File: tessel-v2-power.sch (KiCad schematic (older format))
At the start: 56 parts, among them J301 CONN_01X02, Q301 MMSS8550, U301 AAT4610, U302 AAT4610, U303 AP3417C, U304 AP3417C, U305 AP3418

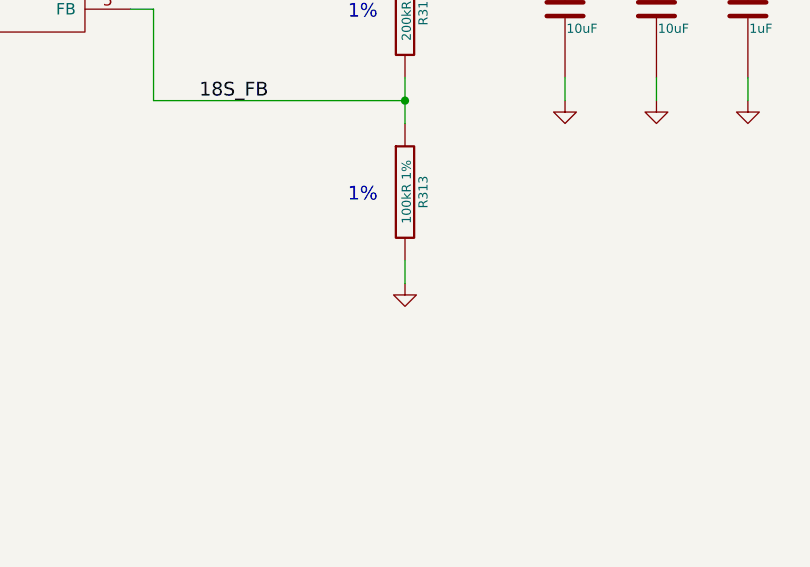
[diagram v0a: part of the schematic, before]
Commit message: swapped led resistor values, package for some dnps, exported to cmp and net
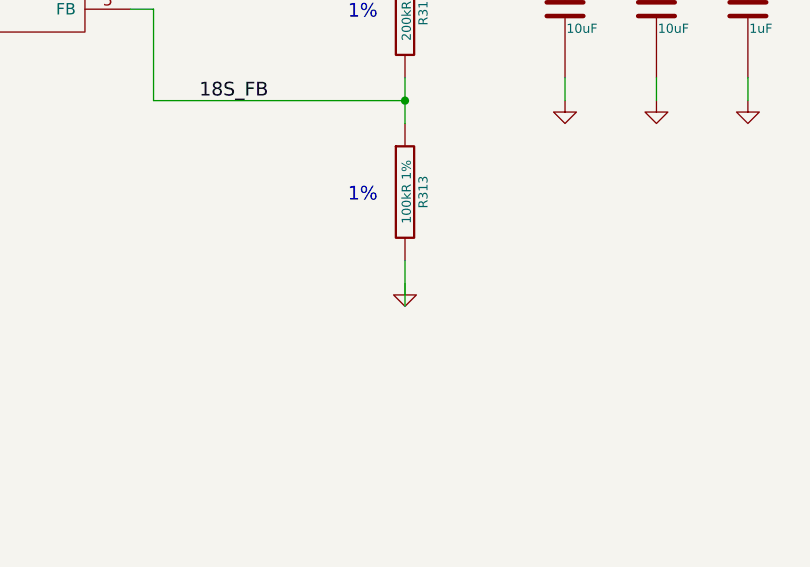
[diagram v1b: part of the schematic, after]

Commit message: led and related resistor changeover
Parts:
- R305, R306: value 1kR -> 120R
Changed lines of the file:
@@
 P 5000 6500
 F 0 "R305" V 5080 6500 40  0000 C CNN
-F 1 "1kR" V 5007 6501 40  0000 C CNN
+F 1 "120R" V 5007 6501 40  0000 C CNN
 F 2 "tm-kicad-lib:SMD-0402-R" V 4930 6500 30  0001 C CNN
 F 3 "" H 5000 6500 30  0000 C CNN
@@
 P 5000 9100
 F 0 "R306" V 5080 9100 40  0000 C CNN
-F 1 "1kR" V 5007 9101 40  0000 C CNN
+F 1 "120R" V 5007 9101 40  0000 C CNN
 F 2 "tm-kicad-lib:SMD-0402-R" V 4930 9100 30  0001 C CNN
 F 3 "" H 5000 9100 30  0000 C CNN

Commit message: swapped load switches
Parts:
- removed U301, U302: AAT4610, Housings_SOT-23_SOT-143_TSOT-6:SOT-23-5, symbol AAT4610
- added U301, U302: MT9700, symbol MT9700
- R303, R304: value 33kR -> 27kR
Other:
- note added: "I_SET = 6.8kV/R_SET\n6.8kV/27kR = 252mA"
- note removed: "R_SET I_LIM\n---------\n56kR : 150mA\n33kR : 250mA\n10kR : 750mA"
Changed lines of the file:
@@
-$EndComp
-$Comp
-L AAT4610 U301
-U 1 1 548FCFA8
-P 3400 5700
-F 0 "U301" H 3050 5950 60  0000 C CNN
-F 1 "AAT4610" H 3400 5700 60  0000 C CNN
-F 2 "Housings_SOT-23_SOT-143_TSOT-6:SOT-23-5" H 3400 5700 60  0001 C CNN
-F 3 "" H 3400 5700 60  0000 C CNN
-	1    3400 5700
-	1    0    0    -1
 $EndComp
 $Comp
@@
 P 2700 6200
 F 0 "R303" V 2780 6200 40  0000 C CNN
-F 1 "33kR" V 2707 6201 40  0000 C CNN
+F 1 "27kR" V 2707 6201 40  0000 C CNN
 F 2 "tm-kicad-lib:SMD-0402-R" V 2630 6200 30  0001 C CNN
 F 3 "" H 2700 6200 30  0000 C CNN
@@
 	1    0    0    -1
 $EndComp
-Text Notes 3050 6400 0    60   ~ 0
-R_SET  I_LIM\n---------\n56kR : 150mA\n33kR : 250mA\n10kR : 750mA
+Text Notes 2900 6300 0    60   ~ 0
+I_SET = 6.8kV/R_SET\n6.8kV/27kR = 252mA
 $Comp
 L TM_C C315
@@
 3.3V_PORT_B
 $Comp
-L AAT4610 U302
-U 1 1 54BD9A8A
-P 3400 8300
-F 0 "U302" H 3050 8550 60  0000 C CNN
-F 1 "AAT4610" H 3400 8300 60  0000 C CNN
-F 2 "Housings_SOT-23_SOT-143_TSOT-6:SOT-23-5" H 3400 8300 60  0001 C CNN
-F 3 "" H 3400 8300 60  0000 C CNN
-	1    3400 8300
-	1    0    0    -1
-$EndComp
-$Comp
 L GND #PWR080
 U 1 1 54BD9A90
@@
 P 2700 8800
 F 0 "R304" V 2780 8800 40  0000 C CNN
-F 1 "33kR" V 2707 8801 40  0000 C CNN
+F 1 "27kR" V 2707 8801 40  0000 C CNN
 F 2 "tm-kicad-lib:SMD-0402-R" V 2630 8800 30  0001 C CNN
 F 3 "" H 2700 8800 30  0000 C CNN
@@
 	1    0    0    -1
 $EndComp
-Text Notes 3050 9000 0    60   ~ 0
-R_SET  I_LIM\n---------\n56kR : 150mA\n33kR : 250mA\n10kR : 750mA
 Text GLabel 2600 8200 0    60   Input ~ 0
 3.3V_CP
@@
 Connection ~ 15300 5700
 Connection ~ 11500 9400
+$Comp
+L MT9700 U301
+U 1 1 5514ACA5
+P 3400 5700
+F 0 "U301" H 3100 5950 60  0000 C CNN
+F 1 "MT9700" H 3400 5700 60  0000 C CNN
+F 2 "" H 3400 5700 60  0000 C CNN
+F 3 "" H 3400 5700 60  0000 C CNN
+	1    3400 5700
+	1    0    0    -1
+$EndComp
+$Comp
+L MT9700 U302
+U 1 1 5514AD5E
+P 3400 8300
+F 0 "U302" H 3100 8550 60  0000 C CNN
+F 1 "MT9700" H 3400 8300 60  0000 C CNN
+F 2 "" H 3400 8300 60  0000 C CNN
+F 3 "" H 3400 8300 60  0000 C CNN
+	1    3400 8300
+	1    0    0    -1
+$EndComp
+Text Notes 2900 8900 0    60   ~ 0
+I_SET = 6.8kV/R_SET\n6.8kV/27kR = 252mA
 $EndSCHEMATC

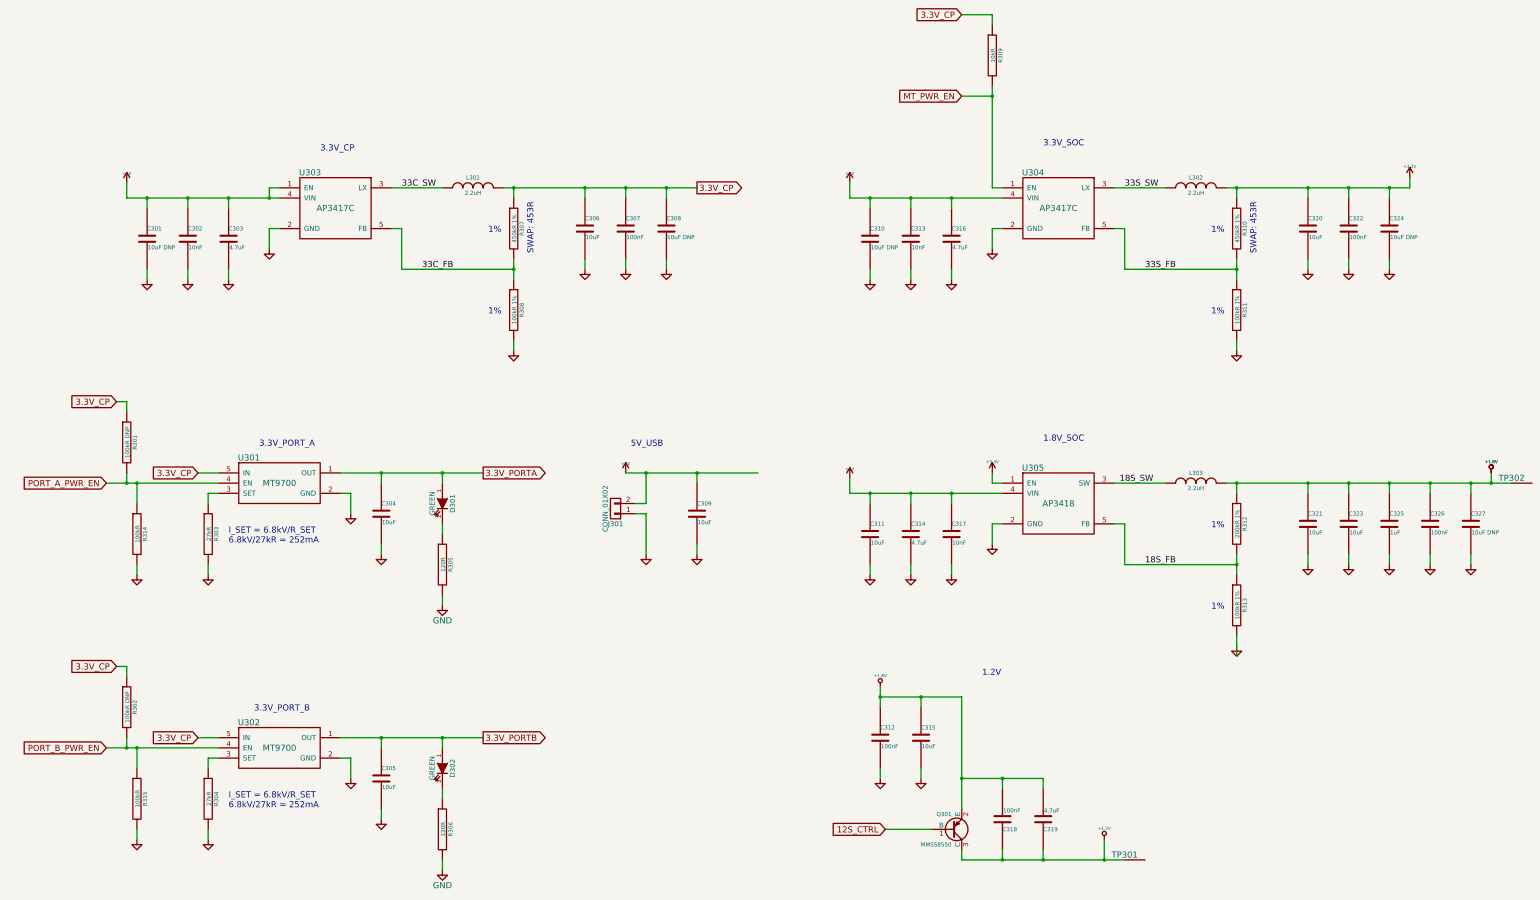
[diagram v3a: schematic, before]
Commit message: swapped to a single 33 regulator...
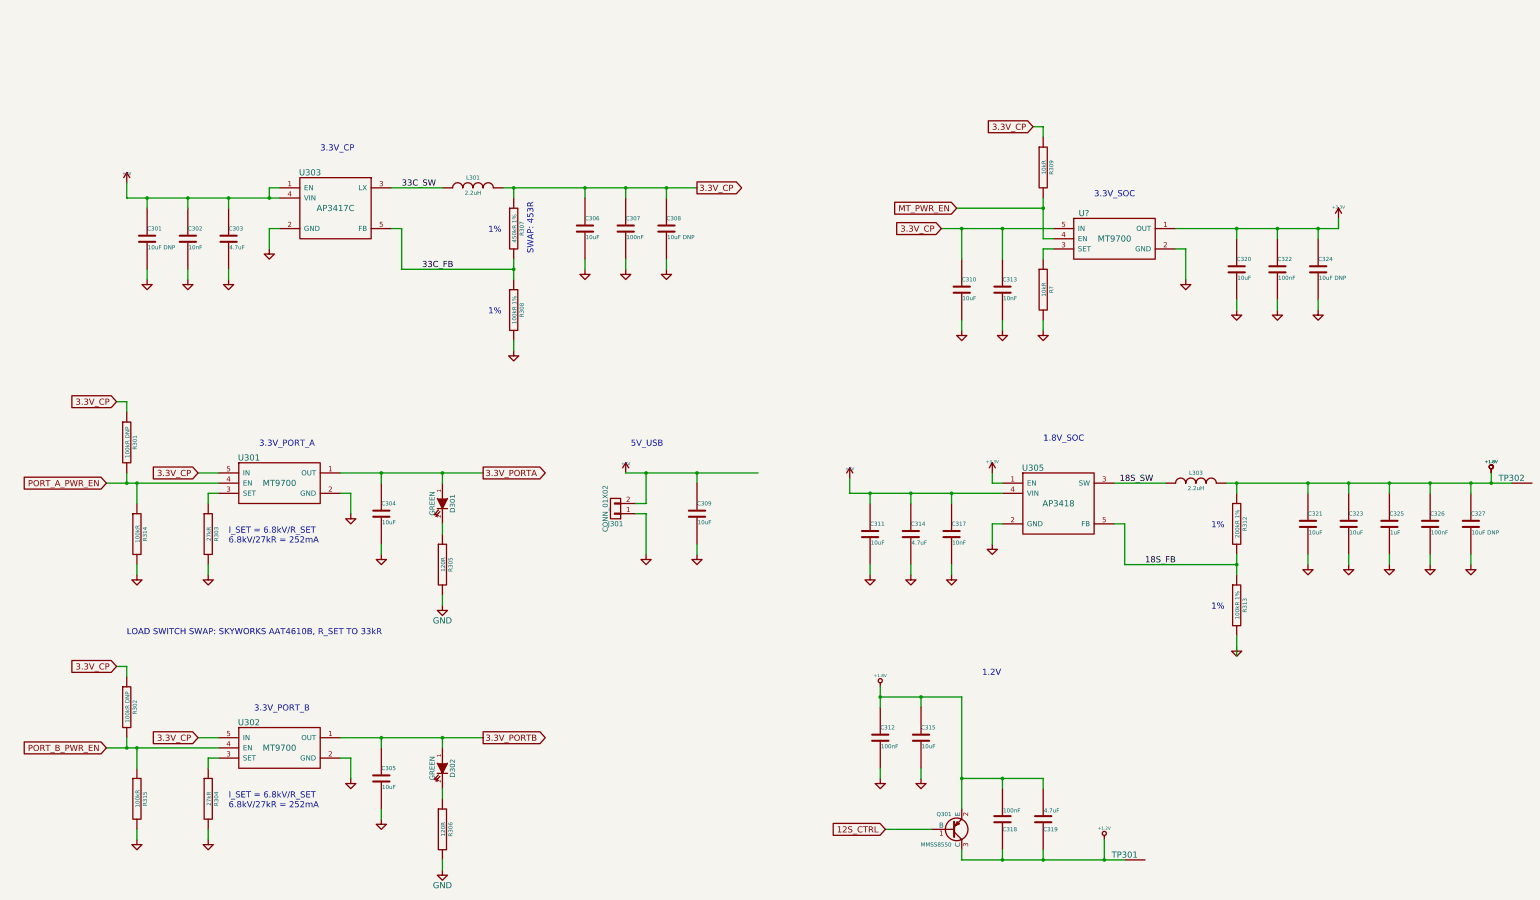
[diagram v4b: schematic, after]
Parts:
- removed C316: 4.7uF, tm-kicad-lib:SMD-0603-C, symbol TM_C
- removed L302: 2.2uH, tm-kicad-lib:SWPA5020S, symbol TM_L
- removed R310: 450kR 1%, tm-kicad-lib:SMD-0402-R, symbol TM_R
- removed R311: 100kR 1%, tm-kicad-lib:SMD-0402-R, symbol TM_R
- removed U304: AP3417C, Housings_SOT-23_SOT-143_TSOT-6:SOT-23-5, symbol AP3417C
- added R?: 10kR, tm-kicad-lib:SMD-0402-R, symbol TM_R
- added U?: MT9700, symbol MT9700
- C310: value 10uF DNP -> 10uF
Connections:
- net +3V3: now also U?.1 (OUT)
- net +5V: no longer C310.1, C313.1
- net 3.3V_CP: now also C310.1, C313.1, U?.5 (IN)
- net GND: now also R?.2, U?.2 (GND)
- net MT_PWR_EN: now also U?.4 (EN)
- new net: R?.1, U?.3 (SET)
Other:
- note added: "LOAD SWITCH SWAP: SKYWORKS AAT4610B, R_SET TO 33kR"
- moved on the sheet: C310, C313, C320, C322, C324, R309

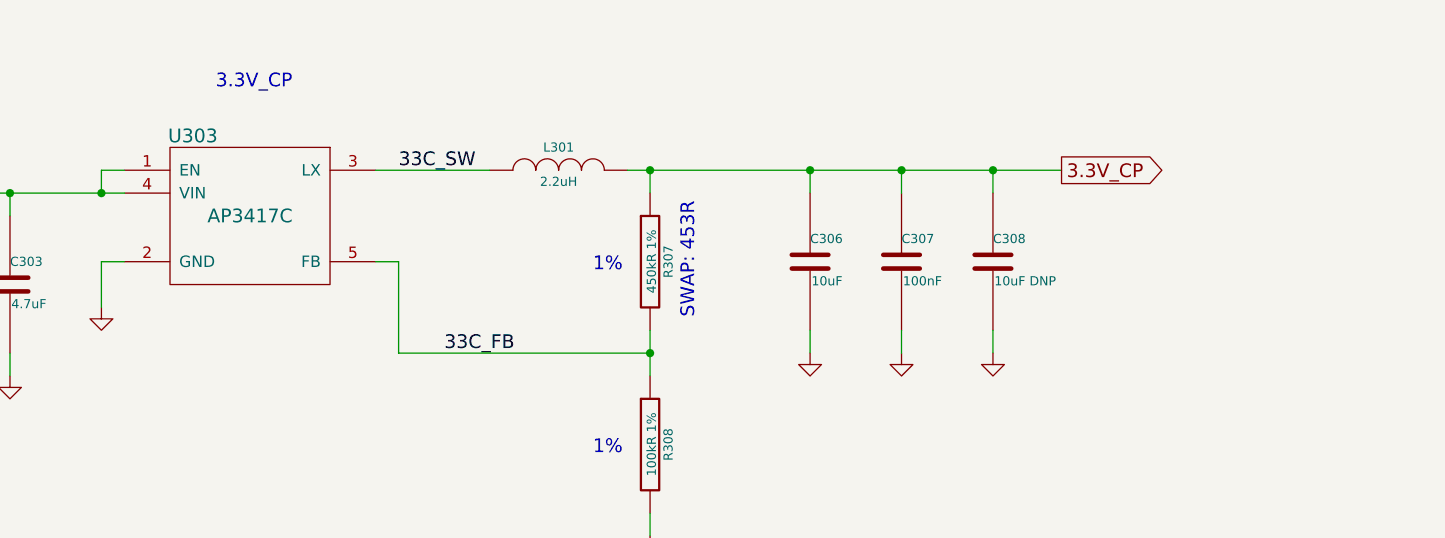
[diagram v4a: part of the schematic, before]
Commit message: more caps
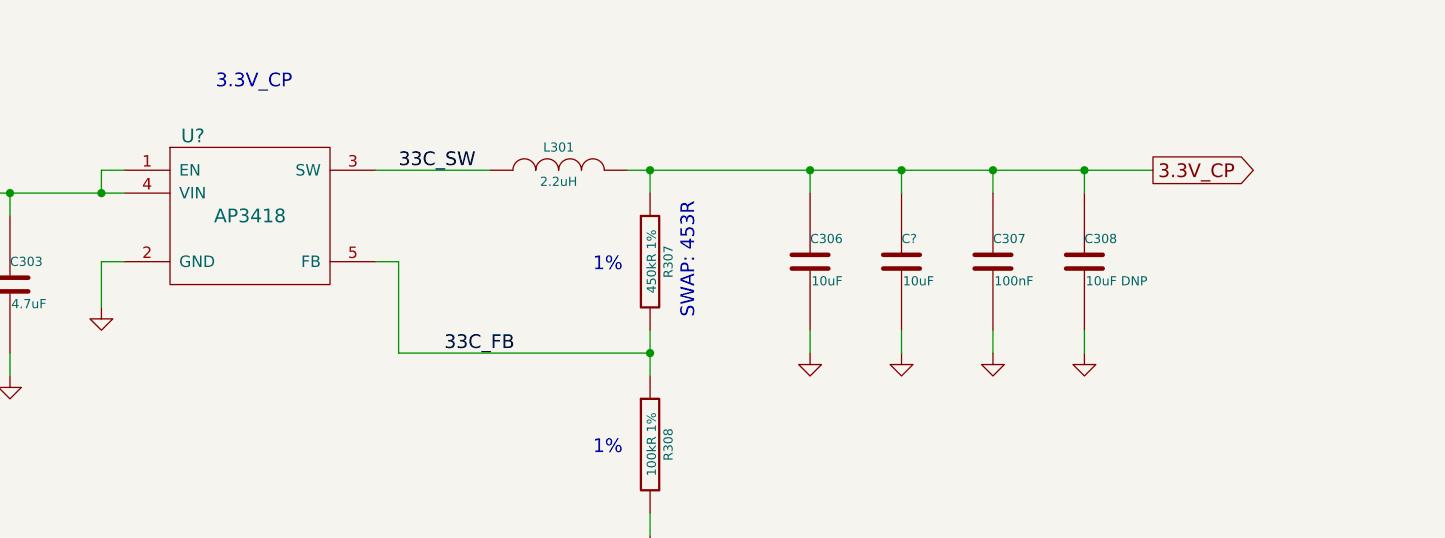
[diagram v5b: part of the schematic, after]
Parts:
- removed U303: AP3417C, Housings_SOT-23_SOT-143_TSOT-6:SOT-23-5, symbol AP3417C
- added C?: 10uF, tm-kicad-lib:SMD-0805-C, symbol TM_C
- added U?: AP3418, Housings_SOT-23_SOT-143_TSOT-6:SOT-23-5, symbol AP3418
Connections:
- net +5V: now also U?.1 (EN), U?.4 (VIN)
- net 3.3V_CP: now also C?.1
- net 33C_FB: now also U?.5 (FB)
- net 33C_SW: now also U?.3 (SW)
- net GND: now also C?.2, U?.2 (GND)
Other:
- moved on the sheet: C307, C308
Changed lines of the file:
@@
 L TM_C C308
 U 1 1 549071E4
-P 7200 3200
-F 0 "C308" H 7200 3300 40  0000 L CNN
-F 1 "10uF DNP" H 7206 3115 40  0000 L CNN
-F 2 "tm-kicad-lib:SMD-0805-C" H 7238 3050 30  0001 C CNN
-F 3 "" H 7200 3200 60  0000 C CNN
-	1    7200 3200
+P 7600 3200
+F 0 "C308" H 7600 3300 40  0000 L CNN
+F 1 "10uF DNP" H 7606 3115 40  0000 L CNN
+F 2 "tm-kicad-lib:SMD-0805-C" H 7638 3050 30  0001 C CNN
+F 3 "" H 7600 3200 60  0000 C CNN
+	1    7600 3200
 	1    0    0    -1
 $EndComp
@@
 L TM_C C307
 U 1 1 549071F0
-P 6800 3200
-F 0 "C307" H 6800 3300 40  0000 L CNN
-F 1 "100nF" H 6806 3115 40  0000 L CNN
-F 2 "tm-kicad-lib:SMD-0402-C" H 6838 3050 30  0001 C CNN
-F 3 "" H 6800 3200 60  0000 C CNN
-	1    6800 3200
+P 7200 3200
+F 0 "C307" H 7200 3300 40  0000 L CNN
+F 1 "100nF" H 7206 3115 40  0000 L CNN
+F 2 "tm-kicad-lib:SMD-0402-C" H 7238 3050 30  0001 C CNN
+F 3 "" H 7200 3200 60  0000 C CNN
+	1    7200 3200
 	1    0    0    -1
 $EndComp
@@
 L GND #PWR065
 U 1 1 54907210
-P 6800 3600
-F 0 "#PWR065" H 6800 3600 30  0001 C CNN
-F 1 "GND" H 6800 3530 30  0001 C CNN
-F 2 "" H 6800 3600 60  0000 C CNN
-F 3 "" H 6800 3600 60  0000 C CNN
-	1    6800 3600
-	1    0    0    -1
-$EndComp
-$Comp
-L GND #PWR066
-U 1 1 54907216
 P 7200 3600
-F 0 "#PWR066" H 7200 3600 30  0001 C CNN
+F 0 "#PWR065" H 7200 3600 30  0001 C CNN
 F 1 "GND" H 7200 3530 30  0001 C CNN
 F 2 "" H 7200 3600 60  0000 C CNN
 F 3 "" H 7200 3600 60  0000 C CNN
 	1    7200 3600
+	1    0    0    -1
+$EndComp
+$Comp
+L GND #PWR066
+U 1 1 54907216
+P 7600 3600
+F 0 "#PWR066" H 7600 3600 30  0001 C CNN
+F 1 "GND" H 7600 3530 30  0001 C CNN
+F 2 "" H 7600 3600 60  0000 C CNN
+F 3 "" H 7600 3600 60  0000 C CNN
+	1    7600 3600
 	1    0    0    -1
 $EndComp
@@
 $EndComp
 $Comp
-L AP3417C U303
-U 1 1 54BDB3A5
-P 3950 3000
-F 0 "U303" H 3700 3350 60  0000 C CNN
-F 1 "AP3417C" H 3950 3000 60  0000 C CNN
-F 2 "Housings_SOT-23_SOT-143_TSOT-6:SOT-23-5" H 3950 3000 60  0001 C CNN
-F 3 "http://diodes.com/datasheets/AP3417C.pdf" H 3950 3000 60  0001 C CNN
-	1    3950 3000
-	1    0    0    -1
-$EndComp
-$Comp
 L GND #PWR083
 U 1 1 54927708
@@
 	1    0    0    -1
 $EndComp
-Text GLabel 7500 2800 2    60   Output ~ 0
+Text GLabel 7900 2800 2    60   Output ~ 0
 3.3V_CP
 $Comp
@@
 Wire Wire Line
 	2100 3000 2100 2900
+Connection ~ 7600 2800
+Wire Wire Line
+	5700 4300 5700 4400
+Wire Wire Line
+	7600 3500 7600 3600
+Wire Wire Line
+	7200 3500 7200 3600
+Wire Wire Line
+	6400 3500 6400 3600
 Connection ~ 7200 2800
 Wire Wire Line
-	5700 4300 5700 4400
-Wire Wire Line
-	7200 3500 7200 3600
-Wire Wire Line
-	6800 3500 6800 3600
-Wire Wire Line
-	6400 3500 6400 3600
-Connection ~ 6800 2800
+	7600 2800 7600 2900
+Connection ~ 6400 2800
 Wire Wire Line
 	7200 2800 7200 2900
-Connection ~ 6400 2800
-Wire Wire Line
-	6800 2800 6800 2900
 Connection ~ 5700 2800
 Wire Wire Line
@@
 	5700 2800 6400 2800
 Wire Wire Line
-	6400 2800 6800 2800
-Wire Wire Line
-	6800 2800 7200 2800
-Wire Wire Line
-	7200 2800 7500 2800
+	6400 2800 7200 2800
+Wire Wire Line
+	7200 2800 7600 2800
+Wire Wire Line
+	7600 2800 7900 2800
 Connection ~ 5700 3600
 Wire Wire Line
@@
 Wire Wire Line
 	12800 3900 12800 4000
+$Comp
+L AP3418 U?
+U 1 1 5514F328
+P 3950 3000
+F 0 "U?" H 3700 3350 60  0000 C CNN
+F 1 "AP3418" H 3950 3000 60  0000 C CNN
+F 2 "Housings_SOT-23_SOT-143_TSOT-6:SOT-23-5" H 3950 3000 60  0001 C CNN
+F 3 "http://diodes.com/datasheets/AP3418.pdf" H 3950 3000 60  0001 C CNN
+	1    3950 3000
+	1    0    0    -1
+$EndComp
+$Comp
+L TM_C C?
+U 1 1 5514F504
+P 6800 3200
+F 0 "C?" H 6800 3300 40  0000 L CNN
+F 1 "10uF" H 6806 3115 40  0000 L CNN
+F 2 "tm-kicad-lib:SMD-0805-C" H 6838 3050 30  0001 C CNN
+F 3 "" H 6800 3200 60  0000 C CNN
+	1    6800 3200
+	1    0    0    -1
+$EndComp
+$Comp
+L GND #PWR?
+U 1 1 5514F50A
+P 6800 3600
+F 0 "#PWR?" H 6800 3600 30  0001 C CNN
+F 1 "GND" H 6800 3530 30  0001 C CNN
+F 2 "" H 6800 3600 60  0000 C CNN
+F 3 "" H 6800 3600 60  0000 C CNN
+	1    6800 3600
+	1    0    0    -1
+$EndComp
+Wire Wire Line
+	6800 3500 6800 3600
+Wire Wire Line
+	6800 2800 6800 2900
+Connection ~ 6800 2800
 $EndSCHEMATC
